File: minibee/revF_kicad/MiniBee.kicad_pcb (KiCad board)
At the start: 2 copper layers, 26.5 x 34 mm, 39 parts, among them IC1 MEGA8-AI, SW1 Switch_SPDT_x2, U1 ADXL345

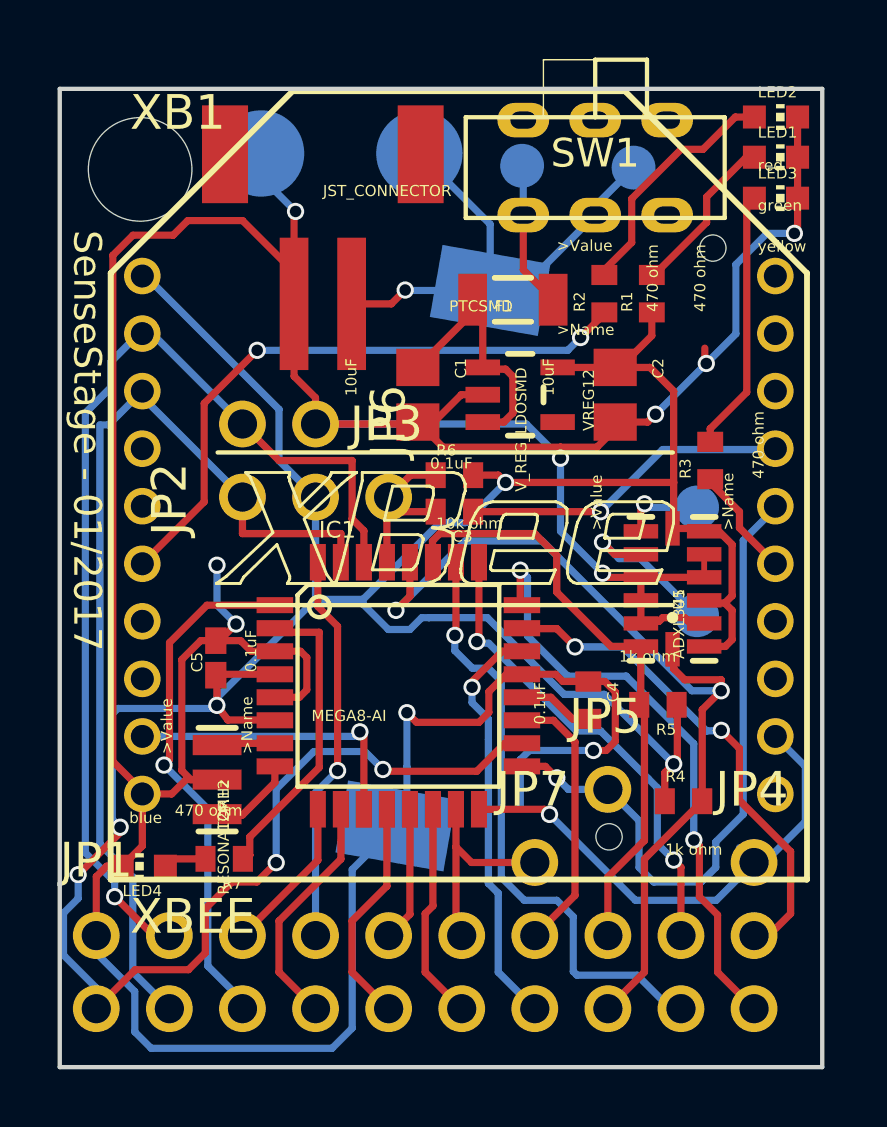
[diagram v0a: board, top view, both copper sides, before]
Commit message: fix some traces (mostly the Vcc trace that was close to the edge)
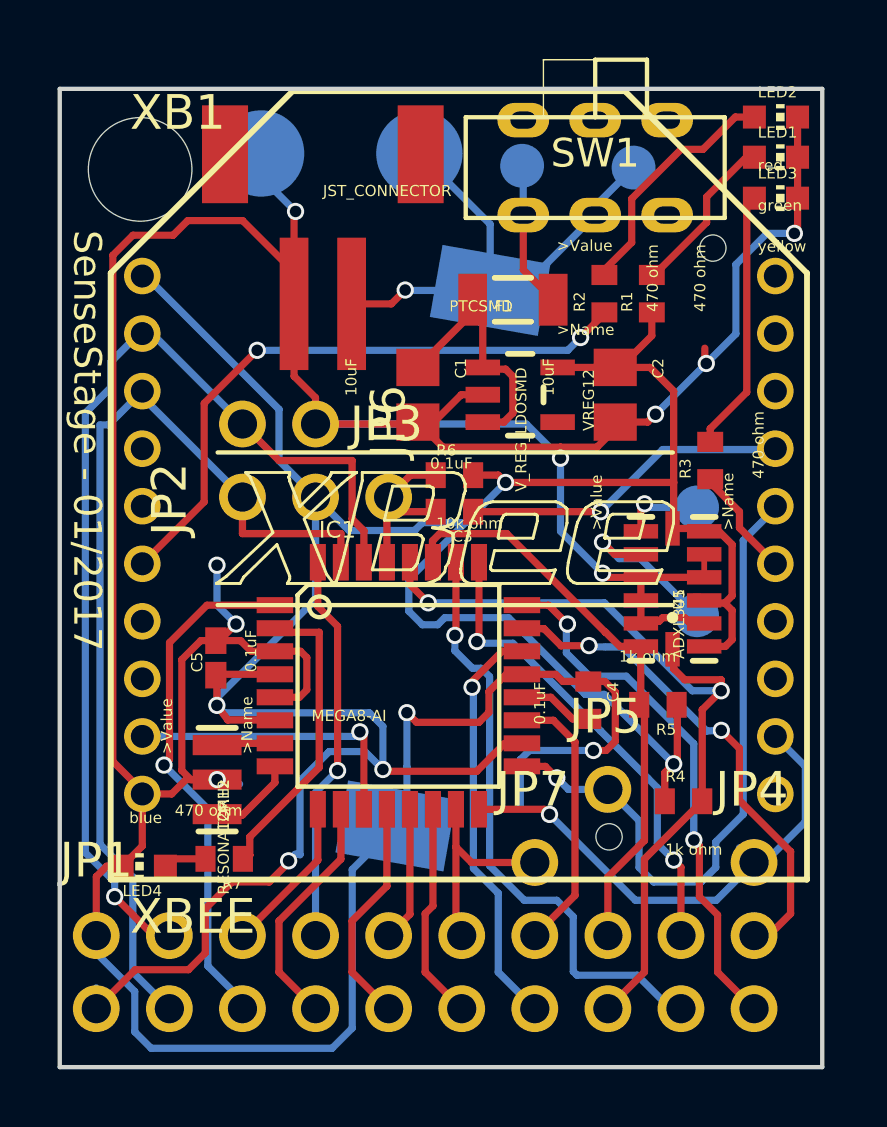
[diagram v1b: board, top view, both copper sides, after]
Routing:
- net VCC: track 113.4 -> 107.7 mm, vias 7 -> 5
- net /SCL: track 31.9 -> 28.7 mm
- net /A1: track 21.0 -> 18.8 mm
- net GND: track 157.0 -> 157.8 mm, vias 10 -> 11
- net /SDA: track 21.1 -> 20.4 mm
